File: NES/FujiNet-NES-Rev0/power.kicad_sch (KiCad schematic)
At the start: 12 parts, among them U12 AP63203WU

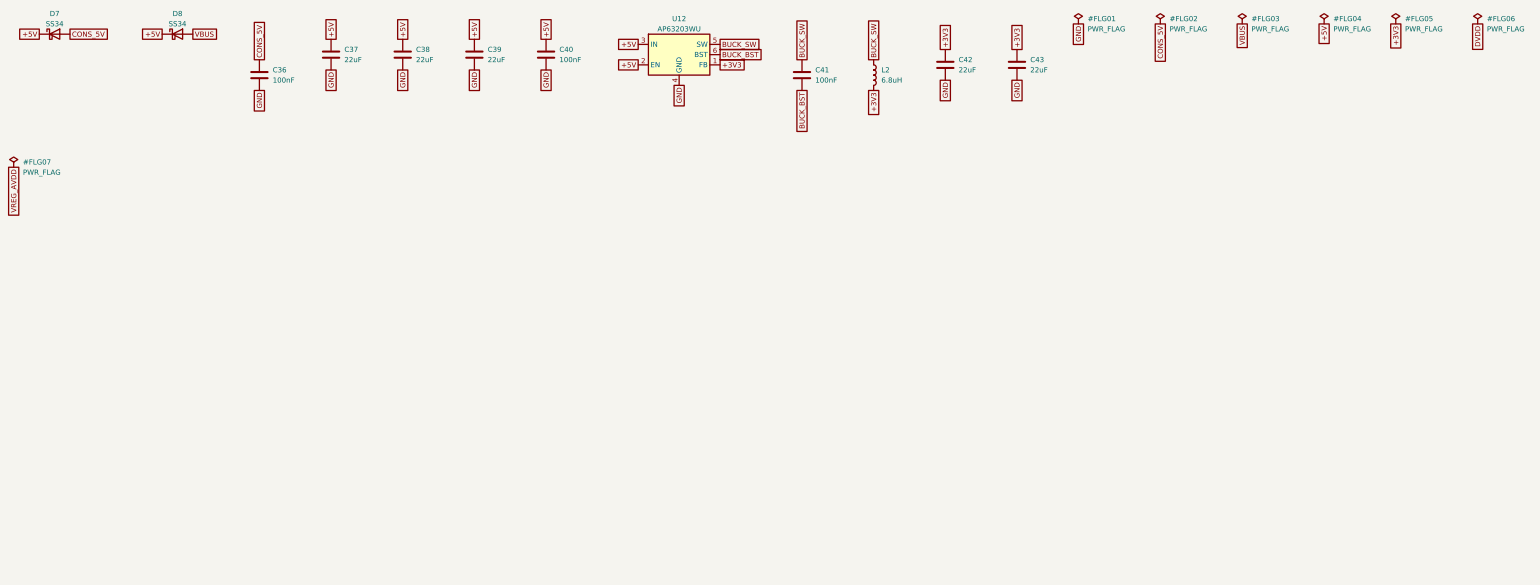
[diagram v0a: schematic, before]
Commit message: Nes rev0 (#48)
* NES: add the FujiNet-NES-Rev0 schematic

RP2354B on the 5 V cart bus with two AS6C4008-55 SRAMs (PRG, CHR) whose
bank lines come from the RP's PIO, 74HCT595/253/14/00/32 glue, and the
Astrocade Rev0 ESP32-S3, USB-UART and power sheets carried over.
Generated from tools/design.py the same way as Astrocade/rev0; ERC
reports no violations and tools/check_nets.py checks every GPIO, SRAM
line and decode equation against fujinet-firmware's nes_cart.h and
fujiversal-nes.h.

Schematic only: no layout, no board built, nothing run on a console.
The edge pinout follows the nesdev Cartridge connector page (pin 37 is
SYSTEM CLK, 2.50 mm pitch).

Co-Authored-By: Claude Fable 5.1 <noreply@anthropic.com>

* NES Rev0: audit the schematic with kicad-happy and redo it

Datasheet-backed review of the first Rev0 schematic (kicad-happy analyzer,
ngspice, 28 deep-review findings all evidence-gated, 453 netlist checks
against fujinet-firmware nes-bringup) and the fixes it called for:

- edge footprint was mirrored (pin 1 west); nesdev and two measured
  NES-EWROM-01 references put pin 1 east on the label side. Fingers are now
  2.0 x 12 mm (ends 3.0 at +/-44.25), 2.50 pitch, copper 1.0-13.0 mm in,
  Nintendo's front/back mask depths
- RP2350 pads are 5 V-tolerant only while IOVDD is powered: the IOVDD group
  moves to an AP2112K (20 us) rail +3V3_RP; VREG_VIN stays on the buck
- 74HCT595 /OE = NAND(PWR_OK, POR) with 100k pull-downs on every bit, so
  the register cannot enable the SRAMs before the RP loads it or while
  the console is off
- PRG /WE = NAND4(M2, ROMSEL, !R/W, PRG_WE_EN) on a CD74HCT20, one gate
  after M2 (was three after the console's /ROMSEL decoder vs ~30 ns hold)
- CIRAM /CE through the 74HCT253's second half, tri-stated by PWR_OK_N
- console 5 V through an AO3401A P-FET (gate = VBUS) instead of a Schottky
- console-sense divider 22k/100k (TI 74HCT14 VT+ reaches 0.70 x VCC)
- WS2812B-2020 on +5V (datasheet VDD 3.7-5.3 V, VIH 2.7 V)
- VBUS decoupling at t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
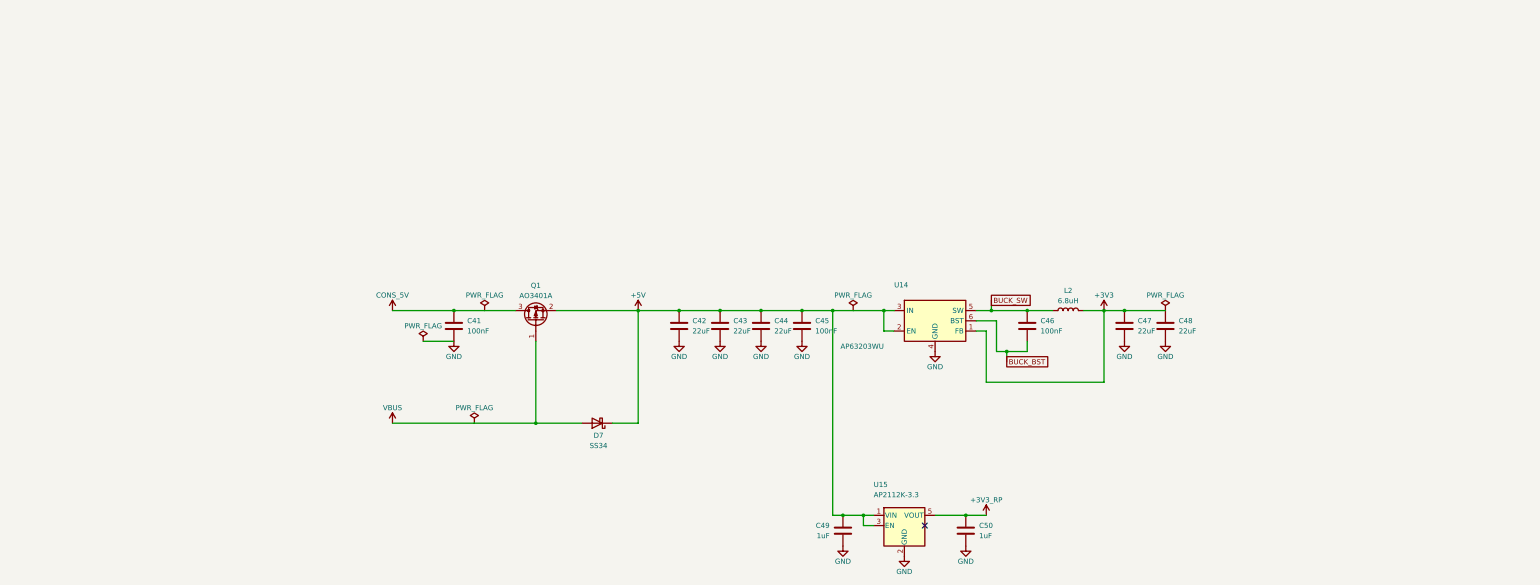
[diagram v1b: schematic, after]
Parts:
- removed C36, C40: 100nF, FujiNet-NES:C_0603_1608Metric, symbol Device:C
- removed C37, C38, C39: 22uF, FujiNet-NES:C_0805_2012Metric, symbol Device:C
- removed D8: SS34, FujiNet-NES:D_SMA, symbol Diode:SS34
- removed U12: AP63203WU, FujiNet-NES:TSOT-23-6, symbol Regulator_Switching:AP63203WU
- added C44, C47, C48: 22uF, FujiNet-NES:C_0805_2012Metric, symbol Device:C
- added C45, C46: 100nF, FujiNet-NES:C_0603_1608Metric, symbol Device:C
- added C49, C50: 1uF, FujiNet-NES:C_0603_1608Metric, symbol Device:C
- added Q1: AO3401A, FujiNet-NES:SOT-23, symbol Transistor_FET:AO3401A
- added U14: AP63203WU, FujiNet-NES:TSOT-23-6, symbol Regulator_Switching:AP63203WU
- added U15: AP2112K-3.3, FujiNet-NES:SOT-23-5, symbol Regulator_Linear:AP2112K-3.3
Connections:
- net +3V3: now also C47.1, C48.1, U14.1 (FB); no longer C42.1, C43.1
- net +5V: now also C42.1, C43.1, C44.1, C45.1, C49.1, Q1.2 (S), U14.2 (EN), U14.3 (IN), U15.1 (VIN), U15.3 (EN)
- net BUCK_BST: now also C46.2, U14.6 (BST); no longer C41.2
- net BUCK_SW: now also C46.1, U14.5 (SW); no longer C41.1
- net CONS_5V: now also C41.1, Q1.3 (D); no longer D7.2 (A)
- net GND: now also C41.2, C44.2, C45.2, C47.2, C48.2, C49.2, C50.2, U14.4 (GND), U15.2 (GND)
- net VBUS: now also D7.2 (A), Q1.1 (G)
- new net +3V3_RP: C50.1, U15.5 (VOUT)
- no-connect marks 0 -> 1
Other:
- title: FujiNet NES Rev0 - Power: console 5V / USB VBUS OR, 3.3V buck -> FujiNet NES Rev0 - Power: 5V OR, 3.3V buck, RP LDO
- moved on the sheet: C41, C42, C43, D7, L2
